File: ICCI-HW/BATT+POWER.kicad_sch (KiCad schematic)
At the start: 59 parts, among them U601 NCV8164ASN180T1G, U602 AP62301WU-7, U603 MAX77962EWJ12+

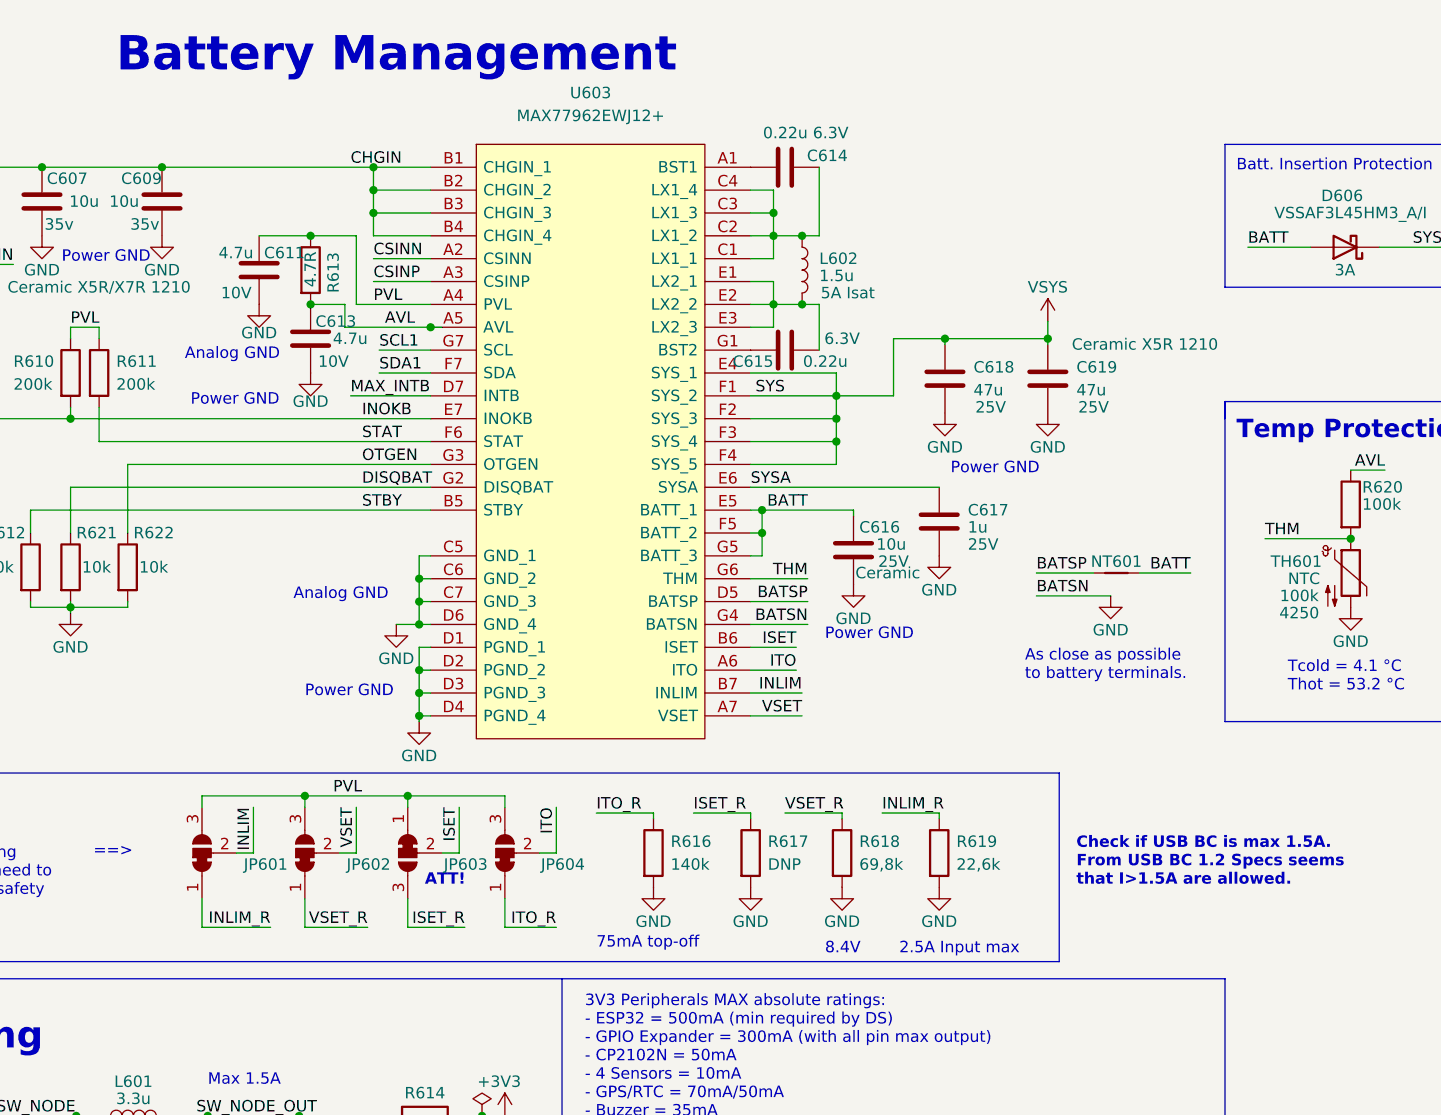
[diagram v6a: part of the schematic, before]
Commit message: change MAX77962 (BGA) to MAX77960B (FC2QFN)
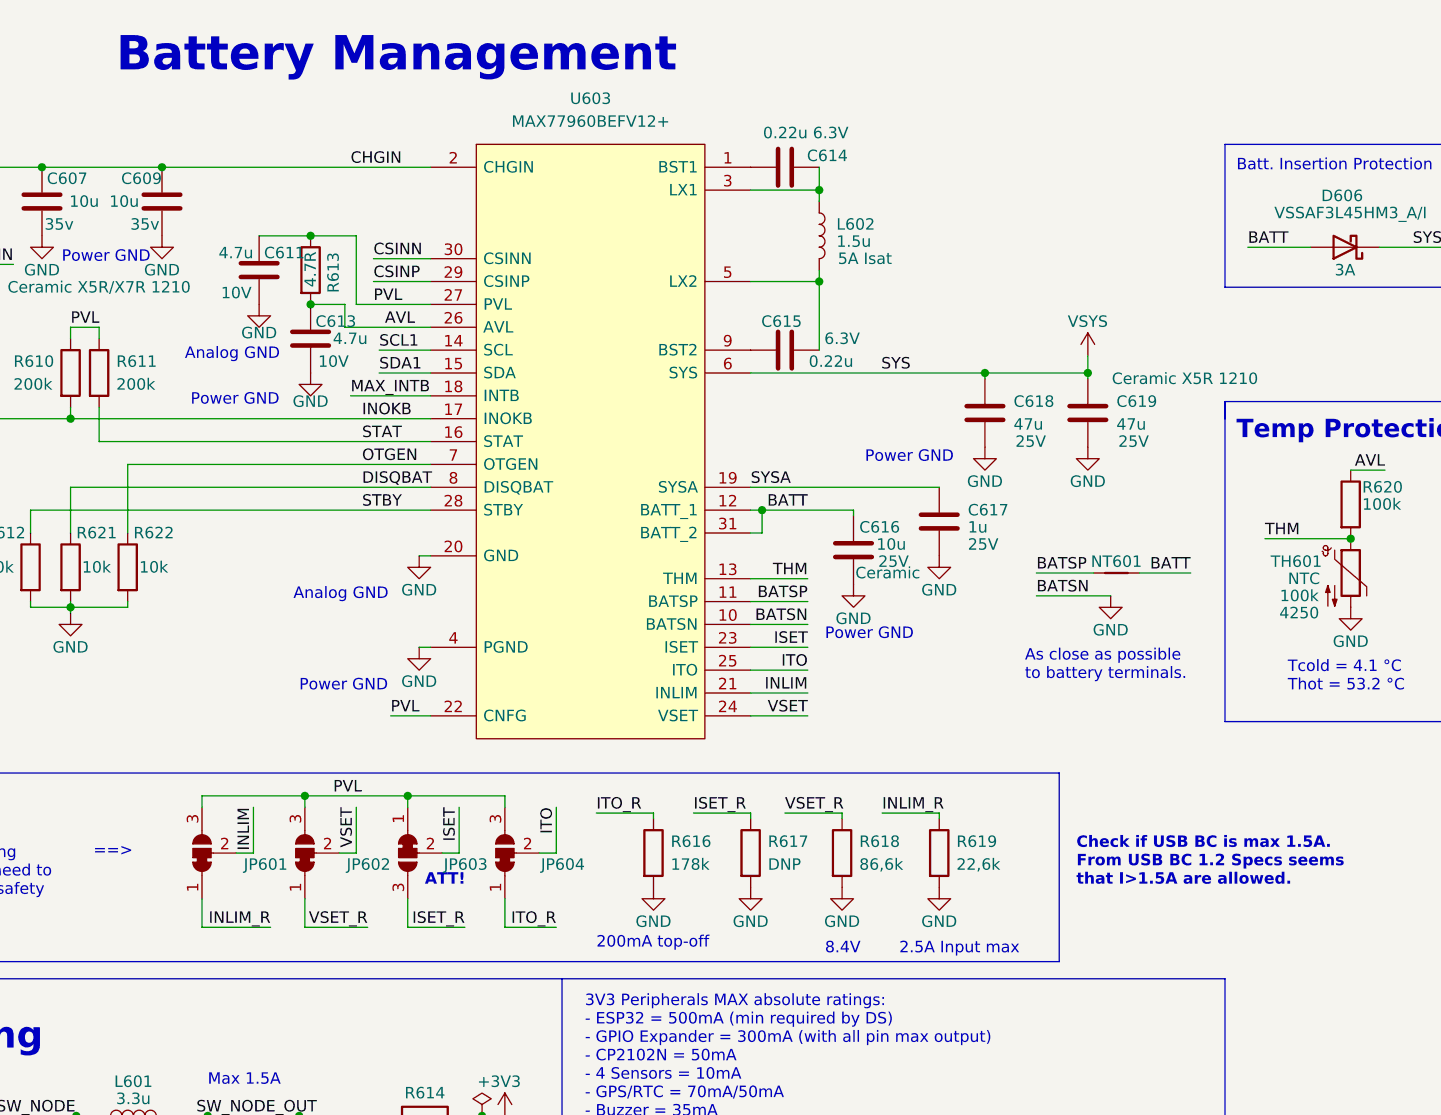
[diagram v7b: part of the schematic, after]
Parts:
- removed U603: MAX77962EWJ12+, ICCI-LIB:MAX77962EWJ12+, symbol ICCI-LIB:MAX77962EWJ12+
- added U603: MAX77960BEFV12+, ICCI-LIB:MAX77960BEFV12+, symbol ICCI-LIB:MAX77960BEFV12+
- R616: value 140k -> 178k
- R618: value 69,8k -> 86,6k
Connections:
- net +BATT: now also U603.12 (BATT_1), U603.31 (BATT_2)
- net AVL: now also U603.26 (AVL)
- net BATSP: now also U603.11 (BATSP)
- net CHGIN: now also U603.2 (CHGIN)
- net CSINN: now also U603.30 (CSINN)
- net CSINP: now also U603.29 (CSINP)
- net DISQBAT: now also U603.8 (DISQBAT)
- net GND: now also U603.10 (BATSN), U603.20 (GND), U603.4 (PGND)
- net INLIM: now also U603.21 (INLIM)
- net ISET: now also U603.23 (ISET)
- net ITO: now also U603.25 (ITO)
- net MAX_INOKB: now also U603.17 (INOKB)
- net MAX_INTB: now also U603.18 (INTB)
- net OTGEN: now also U603.7 (OTGEN)
- net PVL: now also U603.22 (CNFG), U603.27 (PVL)
- net SCL1: now also U603.14 (SCL)
- net SDA1: now also U603.15 (SDA)
- net STAT: now also U603.16 (STAT)
- net STBY: now also U603.28 (STBY)
- net SYSA: now also U603.19 (SYSA)
- net THM: now also U603.13 (THM)
- net VCC: now also U603.6 (SYS)
- net VSET: now also U603.24 (VSET)
- net at C615.1: now also U603.9 (BST2)
- net at C615.2, L602.2: now also U603.5 (LX2)
- net at C614.1: now also U603.1 (BST1)
- net at C614.2, L602.1: now also U603.3 (LX1)
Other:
- note added: "200mA top-off"
- note removed: "75mA top-off"
- moved on the sheet: C618, C619, L602

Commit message: fw: updates
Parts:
- removed BT601: Li-Ion 18650, ICCI-LIB:BAT_1048, symbol Device:Battery_Cell
- added BT601: 2S_Battery 18650, ICCI-LIB:BAT_1048, symbol ICCI-LIB:2S_Battery
- added R623: 100k, Resistor_SMD:R_0603_1608Metric, symbol Device:R
- added SW601: SW_SPDT, ICCI-LIB:OS102011MA1QN1, symbol Switch:SW_SPDT
- C602, C603, C607, C609, C616: footprint Capacitor_SMD:C_0805_2012Metric -> Capacitor_SMD:C_1206_3216Metric
- C618, C619: Voltage 25V -> 25V (16V)
- D601: value 3V3_LED -> BATT_S_LED 5mm Horiz.; footprint LED_SMD:LED_0805_2012Metric -> LED_THT:LED_D5.0mm_Horizontal_O3.81mm_Z3.0mm
- JP601, JP602, JP603, JP604, NT601: now left out of the parts list
- R602: value 510R -> 330R
- R606: value 31,6k -> 31.6k
- R620: renamed from R618; value 86,6k -> 86.6k
- R621: renamed from R619; value 22,6k -> 22.6k
- renumbered D605 to D604, D606 to D605, R612 to R610, R610 to R611, R621 to R612, R611 to R613, R622 to R614, R613 to R616, R614 to R617, R616 to R618, R617 to R619, R620 to R622
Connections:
- net +BATT: now also BT601.C2+; no longer U603.31 (BATT_2)
- net GND: now also BT601.C1-, SW601.3 (C)
- net SW_VIN: now also R623.1
- net at U602.5 (EN): now also SW601.2 (B)
- new net: BT601.C1+, BT601.C2-
- new net: R623.2, SW601.1 (A)
- no-connect marks 1 -> 0
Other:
- note added: "According to the DS, VSYS swings from ABOUT VBATT to VBATTREG= termination voltage=8.4V (Set via I2C or VSET resistor), so from about 6.4 to 8.4"
- note added: "Even if Batt. is not present, VSYS is always regulated to VBATTREG (see datasheet)."
- note removed: "Floating for automatic startup"
- moved on the sheet: C602, D601, D602, D603, F601, R602, R606, R607
